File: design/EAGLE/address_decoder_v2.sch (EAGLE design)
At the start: 18 parts, among them IC1 74LS08N, IC10 MC68010P10, IC11 74LS32N, IC12 74LS21N, IC2 74LS04N, IC3 74LS00N, IC4 74LS21N, IC5 74LS32N, IC6 74LS32N, IC7 74LS02N, IC8 74LS02N, IC9 74LS174N

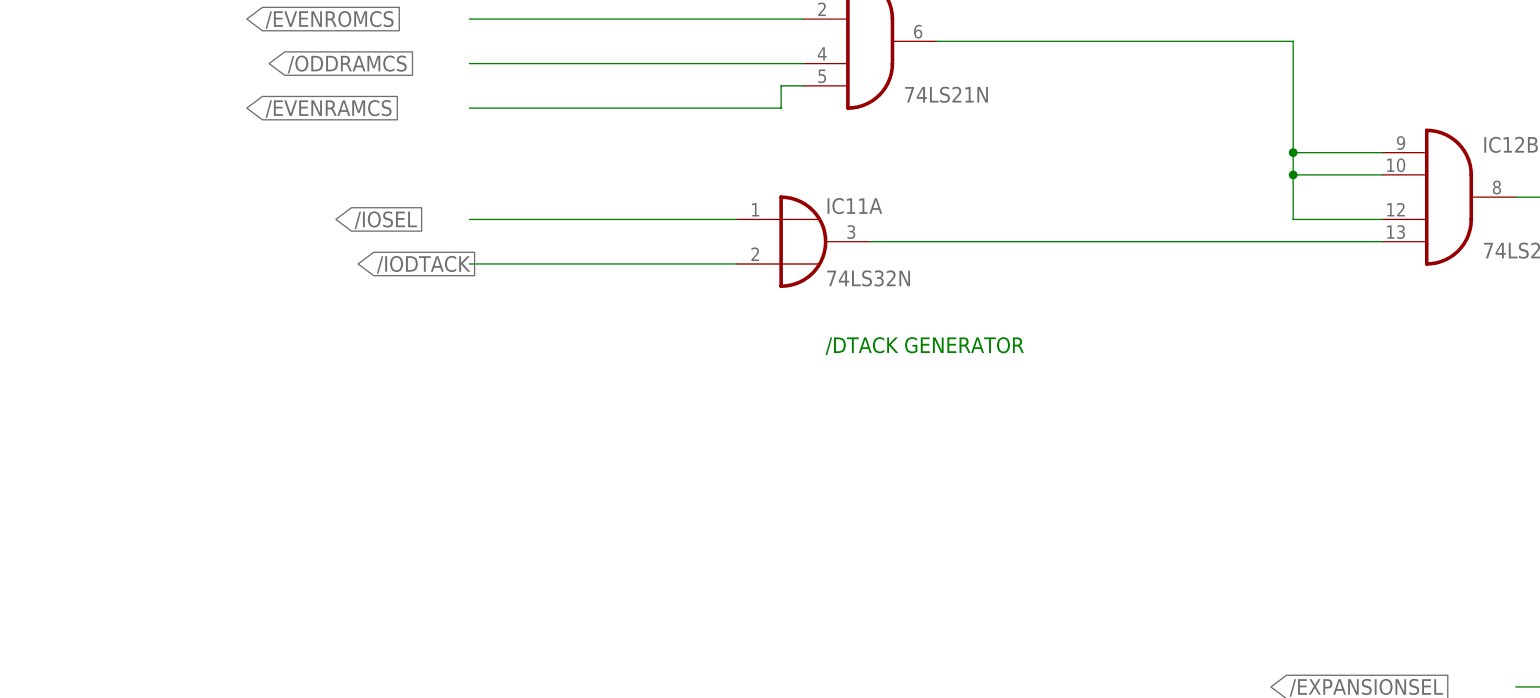
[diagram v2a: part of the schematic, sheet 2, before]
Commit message: Add pullup on DTACK
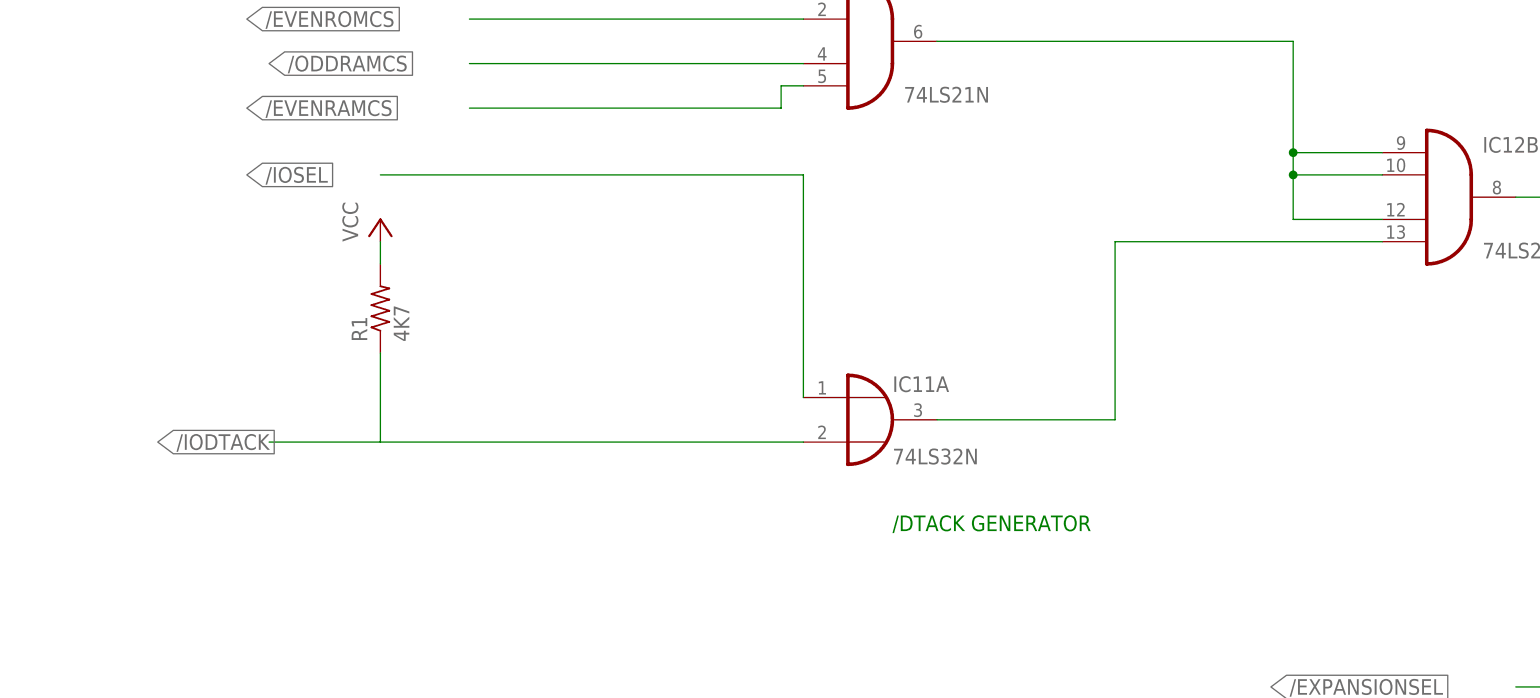
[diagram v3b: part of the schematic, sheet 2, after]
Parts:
- added R1: 4K7, rcl:R-US_0204/7
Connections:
- net /IODTACK: now also R1.1
- net VCC: now also R1.2
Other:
- moved on the sheet: IC11A
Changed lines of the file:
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@@
 <part name="C6" library="capacitor-wima" library_urn="urn:adsk.eagle:library:116" deviceset="C" device="5/3" package3d_urn="urn:adsk.eagle:package:5433/1" value="100nF"/>
 <part name="IC12" library="74xx-eu" library_urn="urn:adsk.eagle:library:85" deviceset="74*21" device="N" package3d_urn="urn:adsk.eagle:package:16407/2" technology="LS"/>
+<part name="P+4" library="supply1" library_urn="urn:adsk.eagle:library:371" deviceset="VCC" device=""/>
+<part name="R1" library="rcl" library_urn="urn:adsk.eagle:library:334" deviceset="R-US_" device="0204/7" package3d_urn="urn:adsk.eagle:package:23498/2" value="4K7"/>
 </parts>
 <sheets>
@@
 <plain>
 <text x="119.38" y="91.44" size="1.778" layer="91">/BOOT LINE GENERATOR</text>
-<text x="195.58" y="177.8" size="1.778" layer="91">/DTACK GENERATOR</text>
+<text x="203.2" y="157.48" size="1.778" layer="91">/DTACK GENERATOR</text>
 </plain>
 <instances>
@@
 <attribute name="VALUE" x="178.435" y="14.605" size="1.778" layer="96"/>
 </instance>
-<instance part="IC11" gate="A" x="193.04" y="190.5" smashed="yes">
-<attribute name="NAME" x="195.58" y="193.675" size="1.778" layer="95"/>
-<attribute name="VALUE" x="195.58" y="185.42" size="1.778" layer="96"/>
+<instance part="IC11" gate="A" x="200.66" y="170.18" smashed="yes">
+<attribute name="NAME" x="203.2" y="173.355" size="1.778" layer="95"/>
+<attribute name="VALUE" x="203.2" y="165.1" size="1.778" layer="96"/>
 </instance>
 <instance part="IC11" gate="P" x="152.4" y="48.26" smashed="yes">
@@
 <instance part="IC12" gate="P" x="165.1" y="48.26" smashed="yes">
 <attribute name="NAME" x="164.465" y="47.625" size="1.778" layer="95"/>
+</instance>
+<instance part="P+4" gate="VCC" x="144.78" y="193.04" smashed="yes">
+<attribute name="VALUE" x="142.24" y="190.5" size="1.778" layer="96" rot="R90"/>
+</instance>
+<instance part="R1" gate="G$1" x="144.78" y="182.88" smashed="yes" rot="R90">
+<attribute name="NAME" x="143.2814" y="179.07" size="1.778" layer="95" rot="R90"/>
+<attribute name="VALUE" x="148.082" y="179.07" size="1.778" layer="96" rot="R90"/>
 </instance>
 </instances>
@@
 <pinref part="IC12" gate="P" pin="VCC"/>
 </segment>
+<segment>
+<pinref part="R1" gate="G$1" pin="2"/>
+<pinref part="P+4" gate="VCC" pin="VCC"/>
+<wire x1="144.78" y1="187.96" x2="144.78" y2="190.5" width="0.1524" layer="91"/>
+</segment>
 </net>
 <net name="N$16" class="0">
@@
 <segment>
 <pinref part="IC11" gate="A" pin="I0"/>
-<wire x1="185.42" y1="193.04" x2="154.94" y2="193.04" width="0.1524" layer="91"/>
-<label x="139.7" y="193.04" size="1.778" layer="95" xref="yes"/>
+<wire x1="193.04" y1="172.72" x2="193.04" y2="198.12" width="0.1524" layer="91"/>
+<label x="129.54" y="198.12" size="1.778" layer="95" xref="yes"/>
+<wire x1="193.04" y1="198.12" x2="144.78" y2="198.12" width="0.1524" layer="91"/>
 </segment>
 </net>
@@
 <segment>
 <pinref part="IC11" gate="A" pin="I1"/>
-<wire x1="185.42" y1="187.96" x2="154.94" y2="187.96" width="0.1524" layer="91"/>
-<label x="142.24" y="187.96" size="1.778" layer="95" xref="yes"/>
-</segment>
-</net>
-<net name="N$32" class="0">
-<segment>
-<pinref part="IC11" gate="A" pin="O"/>
-<wire x1="200.66" y1="190.5" x2="259.08" y2="190.5" width="0.1524" layer="91"/>
-<pinref part="IC12" gate="B" pin="I3"/>
+<label x="119.38" y="167.64" size="1.778" layer="95" xref="yes"/>
+<wire x1="193.04" y1="167.64" x2="144.78" y2="167.64" width="0.1524" layer="91"/>
+<pinref part="R1" gate="G$1" pin="1"/>
+<wire x1="132.08" y1="167.64" x2="144.78" y2="167.64" width="0.1524" layer="91"/>
+<wire x1="144.78" y1="167.64" x2="144.78" y2="177.8" width="0.1524" layer="91"/>
 </segment>
 </net>
@@
 </segment>
 </net>
+<net name="N$24" class="0">
+<segment>
+<pinref part="IC11" gate="A" pin="O"/>
+<wire x1="208.28" y1="170.18" x2="228.6" y2="170.18" width="0.1524" layer="91"/>
+<wire x1="228.6" y1="170.18" x2="228.6" y2="190.5" width="0.1524" layer="91"/>
+<pinref part="IC12" gate="B" pin="I3"/>
+<wire x1="228.6" y1="190.5" x2="259.08" y2="190.5" width="0.1524" layer="91"/>
+</segment>
+</net>

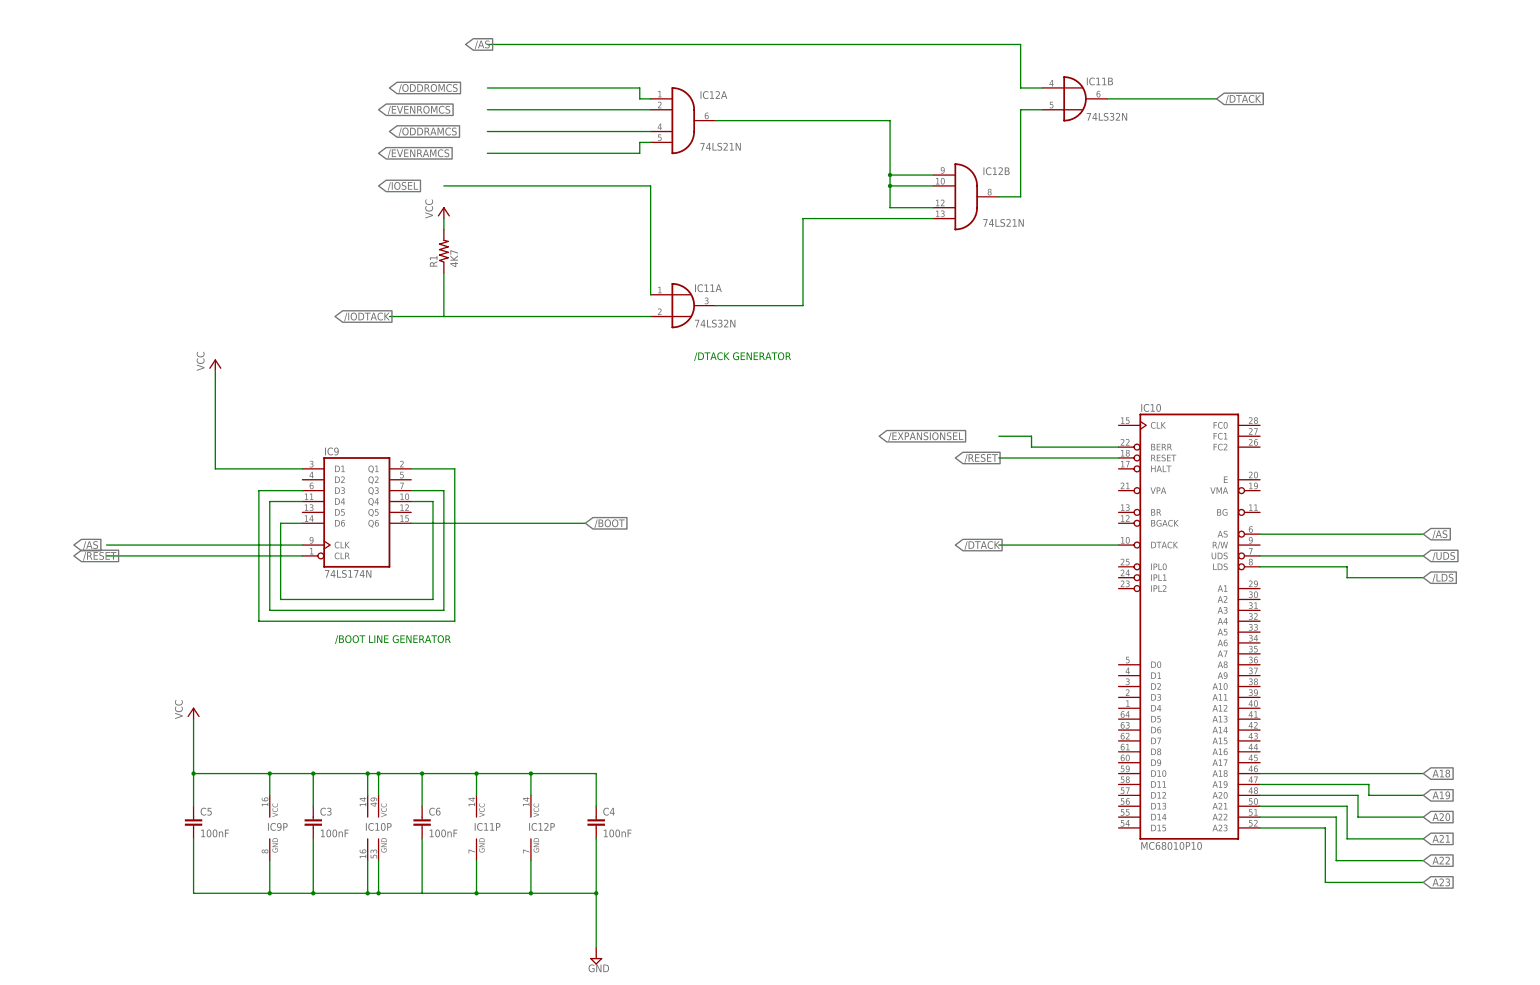
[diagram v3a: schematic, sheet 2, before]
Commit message: New DTACK generator
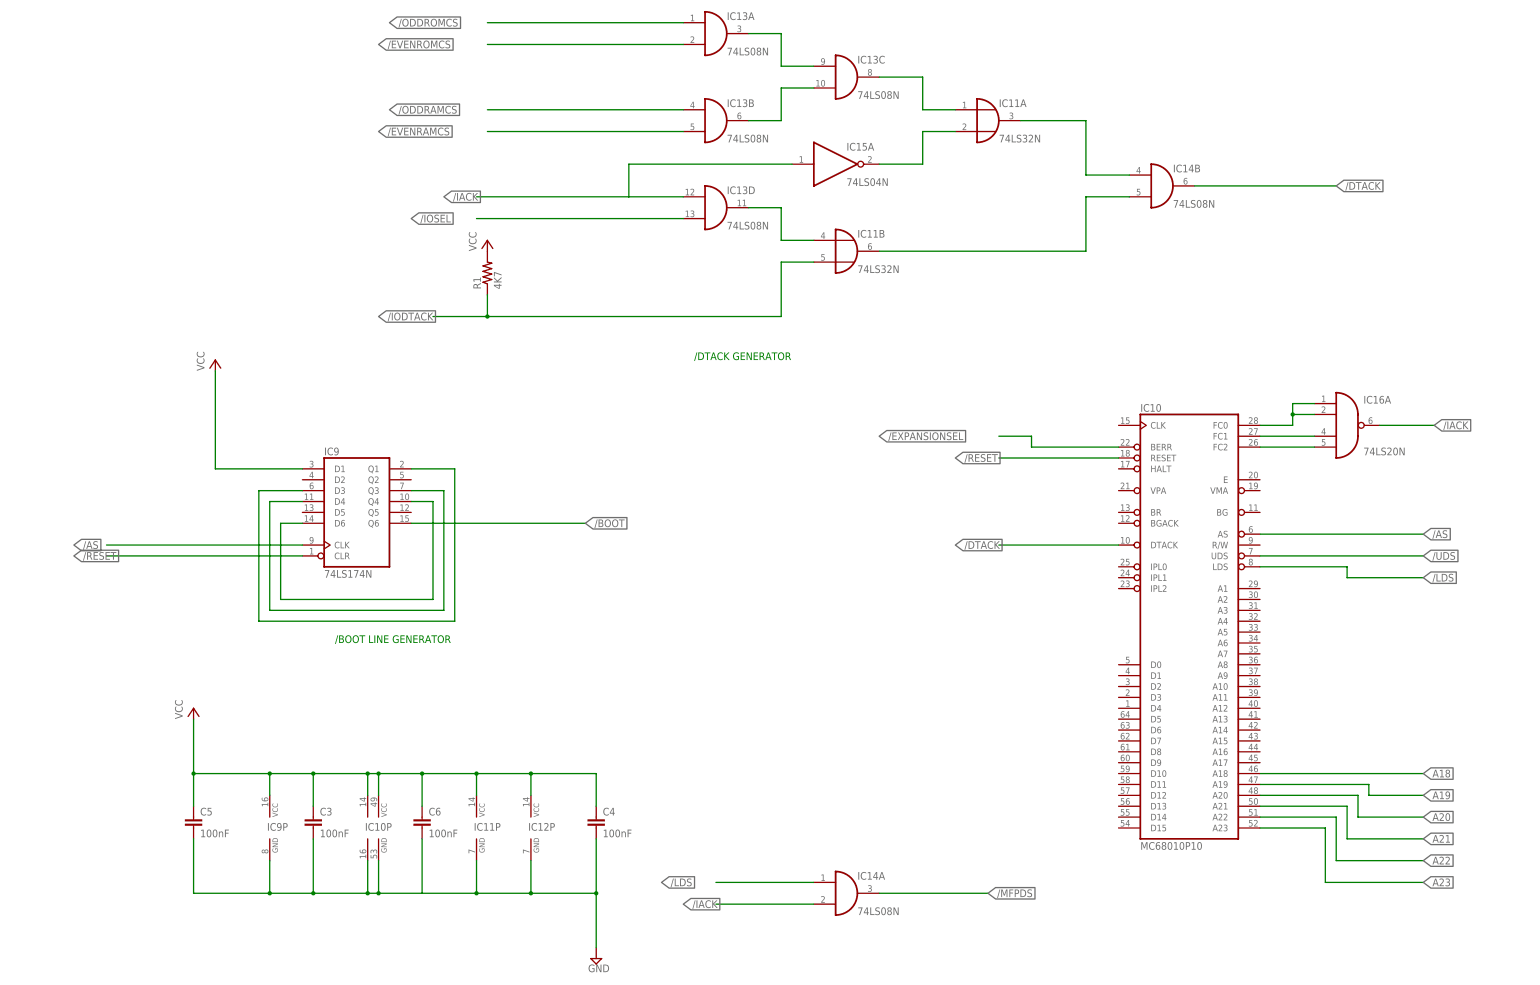
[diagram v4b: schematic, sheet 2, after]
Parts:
- added IC13, IC14: 74LS08N, 74xx-eu:74LS08N
- added IC15: 74LS04N, 74xx-eu:74LS04N
- added IC16: 74LS20N, 74xx-eu:74LS20N
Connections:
- new net /IACK: IC13D.I0, IC14A.I1, IC15A.I, IC16A.O
- new net /MFPDS: IC14A.O
- new net N$25: IC11A.I0, IC13C.O
- new net N$26: IC11A.I1, IC15A.O
- new net N$28: IC11A.O, IC14B.I0
- new net N$29: IC11B.O, IC14B.I1
- new net N$30: IC10G$1.FC2, IC16A.I3
- new net N$31: IC10G$1.FC1, IC16A.I2
- new net N$32: IC10G$1.FC0, IC16A.I0, IC16A.I1
- net /AS: no longer IC11B.I0
- net /DTACK: now also IC14B.O; no longer IC11B.O
- net /EVENRAMCS: now also IC13B.I1; no longer IC12A.I3
- net /EVENROMCS: now also IC13A.I1; no longer IC12A.I1
- net /IODTACK: now also IC11B.I1; no longer IC11A.I1
- net /IOSEL: now also IC13D.I1; no longer IC11A.I0
- net /LDS: now also IC14A.I0
- net /ODDRAMCS: now also IC13B.I0; no longer IC12A.I2
- net /ODDROMCS: now also IC13A.I0; no longer IC12A.I0
- net N$15: now also IC13A.O, IC13C.I0; no longer IC11B.I1, IC12B.O
- net N$24: now also IC13B.O, IC13C.I1; no longer IC11A.O, IC12B.I3
- net N$27: now also IC11B.I0, IC13D.O; no longer IC12A.O, IC12B.I0, IC12B.I1, IC12B.I2
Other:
- moved on the sheet: IC11A, IC11B, R1

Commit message: Finish design of DTACK generator
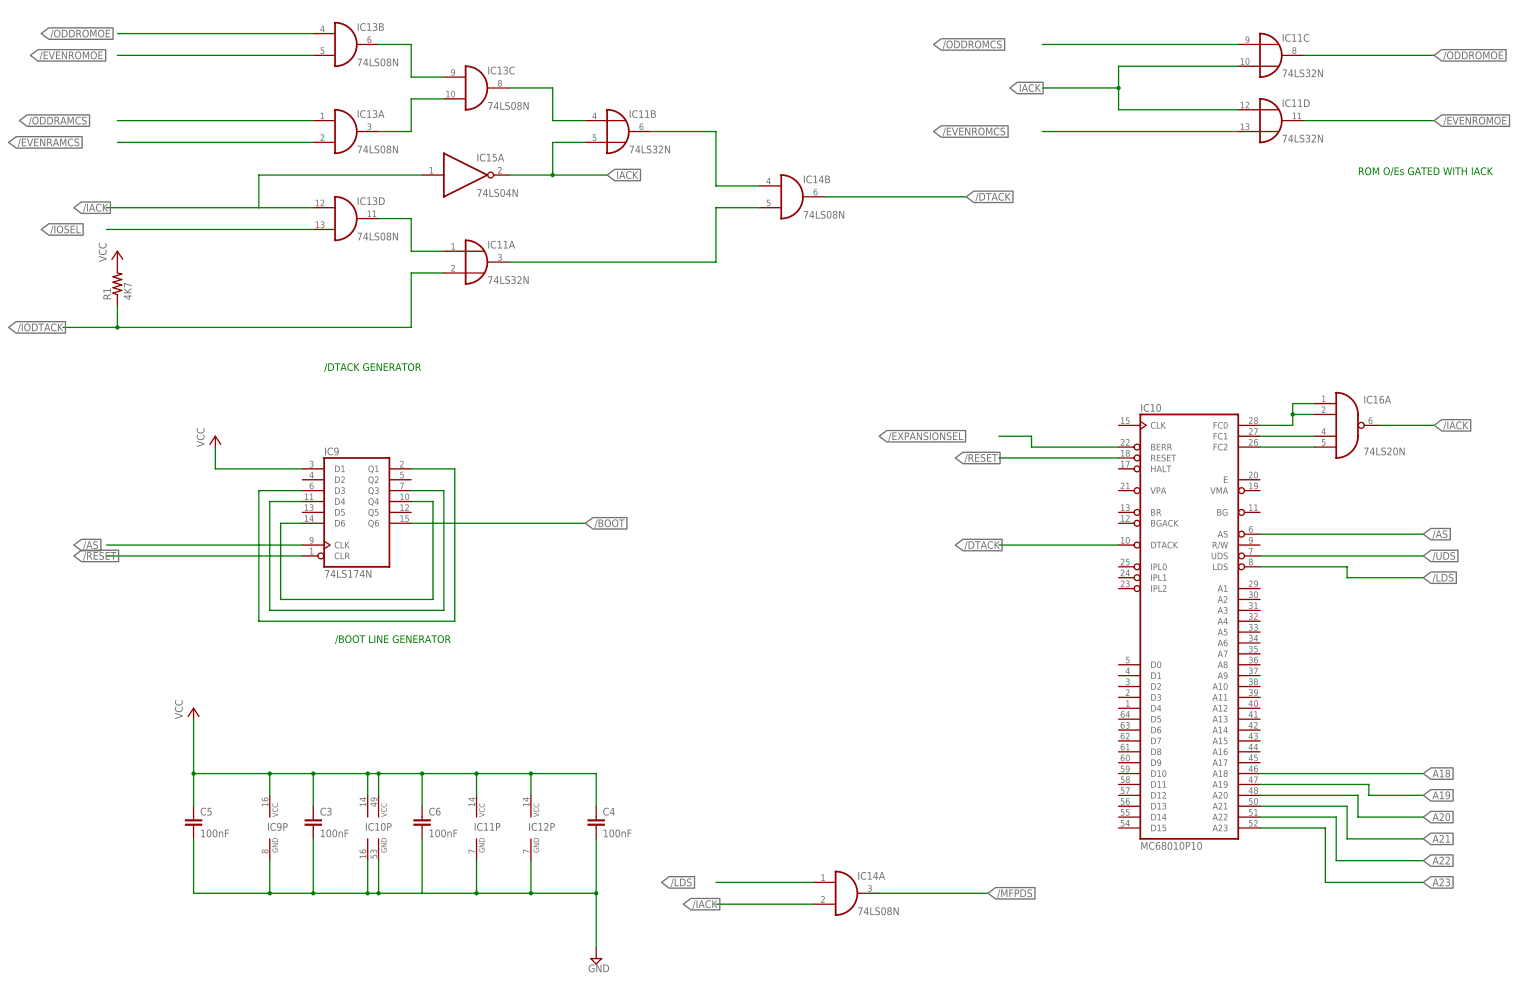
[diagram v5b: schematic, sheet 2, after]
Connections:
- removed net N$26: IC11A.I1, IC15A.O
- new net /EVENROMOE: IC11D.O, IC13B.I1
- new net /ODDROMOE: IC11C.O, IC13B.I0
- new net IACK: IC11B.I1, IC11C.I1, IC11D.I0, IC15A.O
- net /EVENRAMCS: now also IC13A.I1; no longer IC13B.I1
- net /EVENROMCS: now also IC11D.I1; no longer IC13A.I1
- net /IODTACK: now also IC11A.I1; no longer IC11B.I1
- net /ODDRAMCS: now also IC13A.I0; no longer IC13B.I0
- net /ODDROMCS: now also IC11C.I0; no longer IC13A.I0
- net N$15: now also IC13B.O; no longer IC13A.O
- net N$24: now also IC13A.O; no longer IC13B.O
- net N$25: now also IC11B.I0; no longer IC11A.I0
- net N$27: now also IC11A.I0; no longer IC11B.I0
- net N$28: now also IC11B.O; no longer IC11A.O
- net N$29: now also IC11A.O; no longer IC11B.O
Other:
- note added: "ROM O/Es GATED WITH IACK"
- moved on the sheet: IC11A, IC11B, IC13A, IC13B, IC13C, IC13D, IC14B, IC15A, R1
